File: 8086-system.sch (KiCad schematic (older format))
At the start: 2 parts

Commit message: created 8284A clock generator block
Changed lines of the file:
@@
 $Descr A4 11693 8268
 encoding utf-8
-Sheet 1 3
+Sheet 1 4
 Title "8086-system"
 Date ""
@@
 F0 "external-connectors" 50
 F1 "external-connectors.sch" 50
-F2 "ADDRESS_BUS" O L 8950 3100 50
-F3 "CLK" I L 8950 3450 50
-F4 "~BHE" I L 8950 3600 50
-F5 "~MRDC" I R 9900 3250 50
-F6 "~MWTC" I R 9900 3350 50
-F7 "~IORC" I R 9900 3450 50
-F8 "~IOWC" I R 9900 3550 50
-F9 "DATA_BUS" B L 8950 3200 50
+F2 "CLK" I L 8950 3500 50
+F3 "~BHE" I L 8950 3300 50
+F4 "~MRDC" I R 9900 3250 50
+F5 "~MWTC" I R 9900 3350 50
+F6 "~IORC" I R 9900 3450 50
+F7 "~IOWC" I R 9900 3550 50
+F8 "DATA_BUS" B L 8950 3200 50
+F9 "RESET" I L 8950 3600 50
+F10 "ADDRESS_BUS" I L 8950 3100 50
 $EndSheet
 Text Label 2000 3350 0    50   ~ 0
@@
 Text Label 1150 3400 2    50   ~ 0
 RESET
-Text Label 1150 3600 2    50   ~ 0
-~TEST
 Text Label 1150 3700 2    50   ~ 0
 HOLD
@@
 Text Label 1150 4200 2    50   ~ 0
 ~INTA
-Text Label 8950 3450 2    50   ~ 0
+Text Label 8950 3500 2    50   ~ 0
 CLK
-Text Label 8950 3600 2    50   ~ 0
+Text Label 8950 3300 2    50   ~ 0
 ~BHE
 Text Label 9900 3250 0    50   ~ 0
@@
 $EndComp
 $Comp
-L power:GND #PWR?
+L power:GND #PWR0101
 U 1 1 62850EC1
 P 1500 7450
-F 0 "#PWR?" H 1500 7200 50  0001 C CNN
+F 0 "#PWR0101" H 1500 7200 50  0001 C CNN
 F 1 "GND" H 1505 7277 50  0000 C CNN
 F 2 "" H 1500 7450 50  0001 C CNN
@@
 $EndComp
 $Comp
-L power:VCC #PWR?
+L power:VCC #PWR0102
 U 1 1 62851416
 P 1900 7150
-F 0 "#PWR?" H 1900 7000 50  0001 C CNN
+F 0 "#PWR0102" H 1900 7000 50  0001 C CNN
 F 1 "VCC" H 1915 7323 50  0000 C CNN
 F 2 "" H 1900 7150 50  0001 C CNN
@@
 	1350 7450 1500 7450
 Connection ~ 1500 7450
+$Sheet
+S 1700 1050 750  550
+U 6193175A
+F0 "clock-generator" 50
+F1 "clock-generator.sch" 50
+F2 "PCLK" O R 2450 1250 50
+F3 "CLK" O R 2450 1150 50
+F4 "RESET" O R 2450 1400 50
+F5 "READY" O R 2450 1500 50
+F6 "RDY1" I L 1700 1150 50
+F7 "RDY2" I L 1700 1400 50
+$EndSheet
+Text Label 2450 1150 0    50   ~ 0
+CLK
+Text Label 2450 1250 0    50   ~ 0
+PCLK
+Text Label 2450 1500 0    50   ~ 0
+READY
+Text Label 2450 1400 0    50   ~ 0
+RESET
+Wire Wire Line
+	1150 3600 800  3600
+$Comp
+L power:GND #PWR0103
+U 1 1 61966AE7
+P 800 3600
+F 0 "#PWR0103" H 800 3350 50  0001 C CNN
+F 1 "GND" H 805 3427 50  0000 C CNN
+F 2 "" H 800 3600 50  0001 C CNN
+F 3 "" H 800 3600 50  0001 C CNN
+	1    800  3600
+	1    0    0    -1
+$EndComp
+Wire Wire Line
+	1400 1150 1400 1400
+$Comp
+L power:VCC #PWR0104
+U 1 1 61967609
+P 1400 1150
+F 0 "#PWR0104" H 1400 1000 50  0001 C CNN
+F 1 "VCC" H 1415 1323 50  0000 C CNN
+F 2 "" H 1400 1150 50  0001 C CNN
+F 3 "" H 1400 1150 50  0001 C CNN
+	1    1400 1150
+	1    0    0    -1
+$EndComp
+Wire Wire Line
+	1700 1400 1400 1400
+Wire Wire Line
+	1700 1150 1400 1150
+Connection ~ 1400 1150
+Text Label 8950 3600 2    50   ~ 0
+RESET
 $EndSCHEMATC

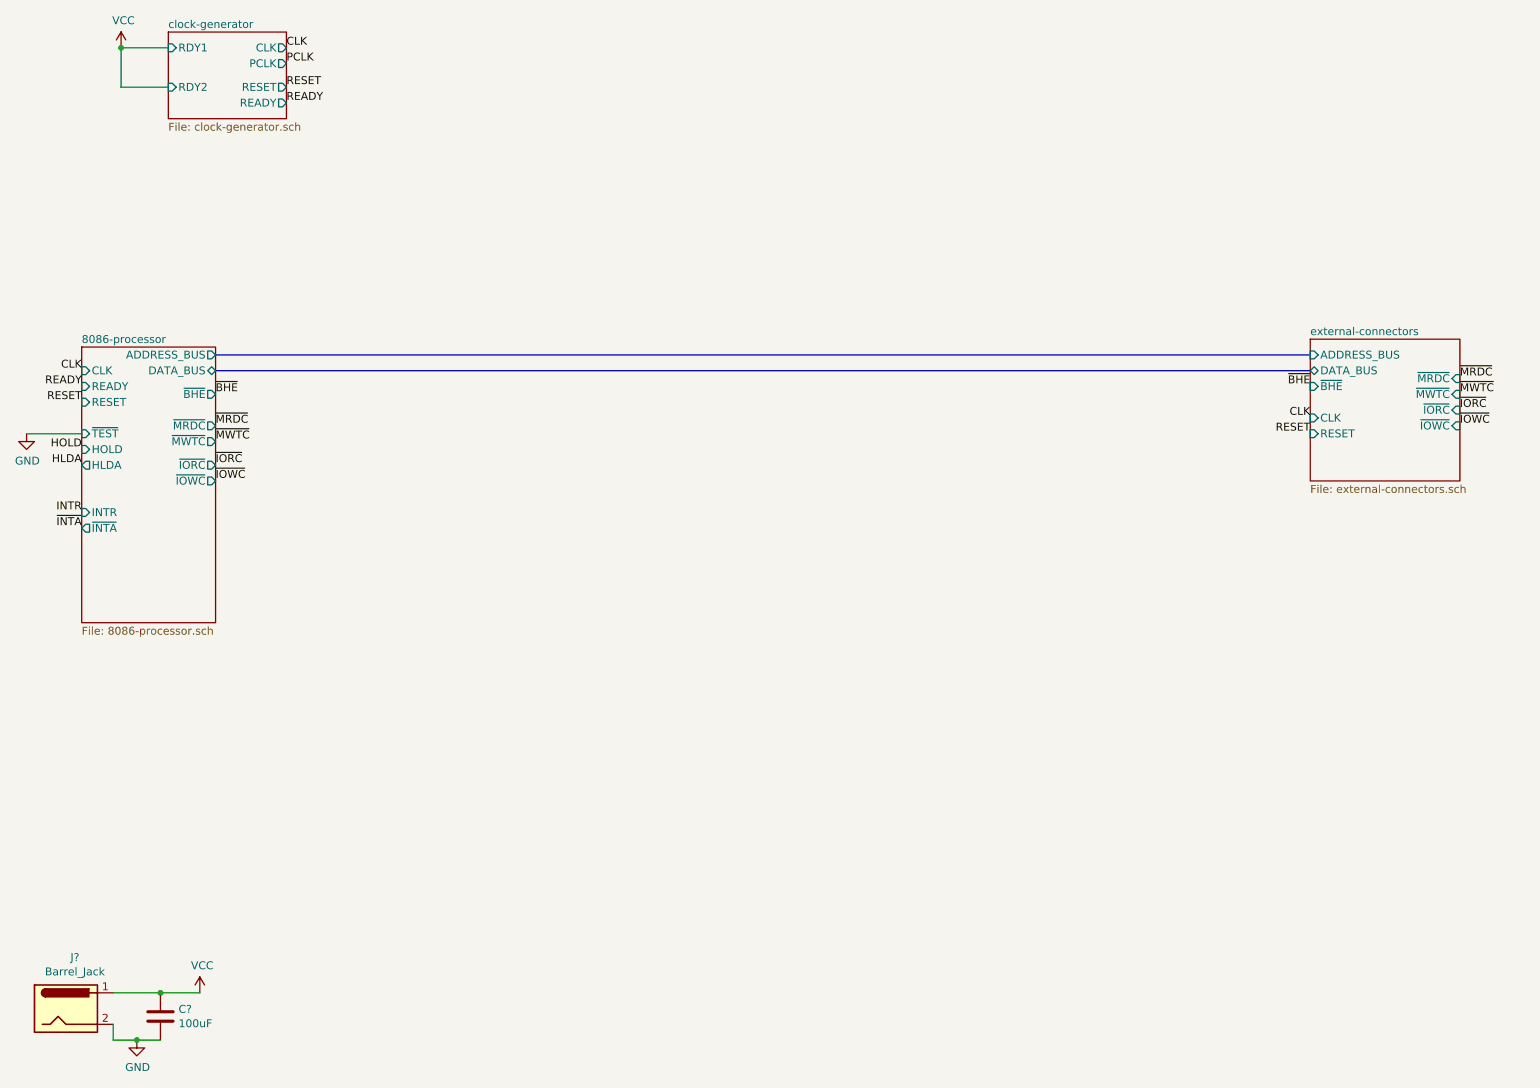
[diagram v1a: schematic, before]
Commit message: created 28F010 CMOS flash block; improved power decoupling; added M/~IO pin from 8086 sheet; reduced no. of logic gates in 8086 processor block; added +12V; moved input power to external-connectors sheet; annotated schematics
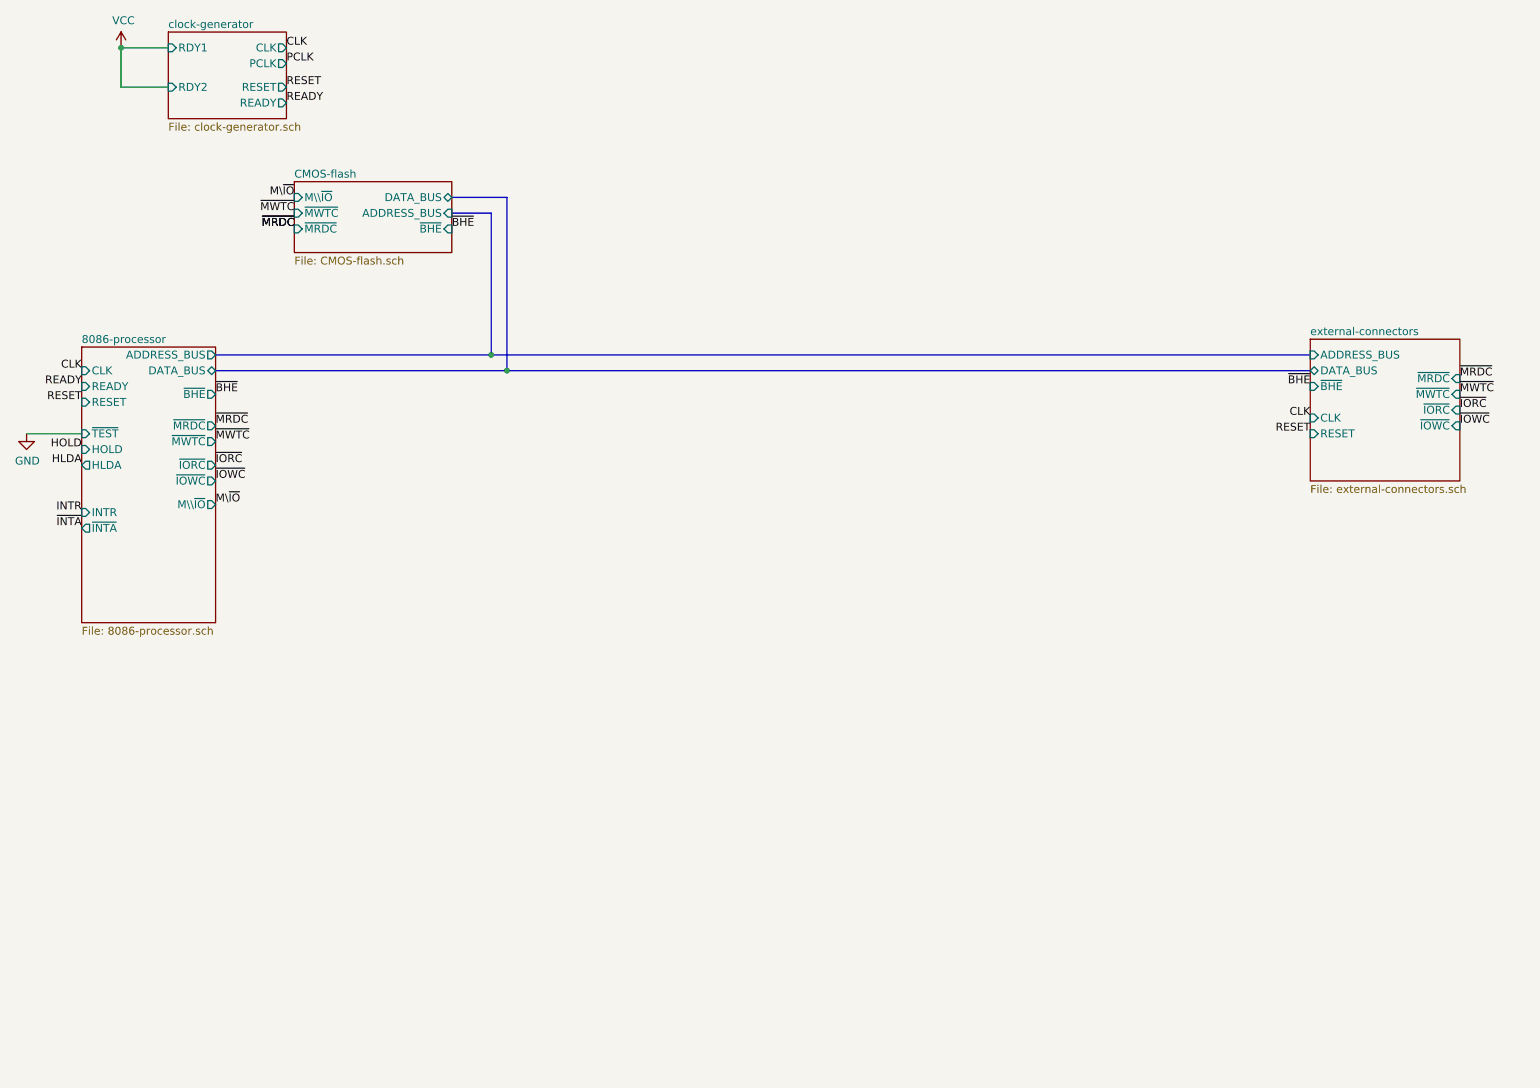
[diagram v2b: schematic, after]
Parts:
- removed C?: 100uF, symbol Device:C
- removed J?: Barrel_Jack, symbol Connector:Barrel_Jack
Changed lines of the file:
@@
 $Descr A4 11693 8268
 encoding utf-8
-Sheet 1 4
+Sheet 1 5
 Title "8086-system"
 Date ""
@@
 F15 "~IOWC" O R 2000 3900 50
 F16 "DATA_BUS" B R 2000 3200 50
+F17 "M\\~IO" O R 2000 4050 50
 $EndSheet
 $Sheet
@@
 ~IOWC
 Wire Bus Line
-	2000 3100 8950 3100
+	2000 3100 3750 3100
 Wire Bus Line
-	2000 3200 8950 3200
-$Comp
-L Connector:Barrel_Jack J?
-U 1 1 6284FC4C
-P 1050 7250
-F 0 "J?" H 1107 7575 50  0000 C CNN
-F 1 "Barrel_Jack" H 1107 7484 50  0000 C CNN
-F 2 "" H 1100 7210 50  0001 C CNN
-F 3 "~" H 1100 7210 50  0001 C CNN
-	1    1050 7250
-	1    0    0    -1
-$EndComp
-$Comp
-L power:GND #PWR0101
-U 1 1 62850EC1
-P 1500 7450
-F 0 "#PWR0101" H 1500 7200 50  0001 C CNN
-F 1 "GND" H 1505 7277 50  0000 C CNN
-F 2 "" H 1500 7450 50  0001 C CNN
-F 3 "" H 1500 7450 50  0001 C CNN
-	1    1500 7450
-	1    0    0    -1
-$EndComp
-$Comp
-L power:VCC #PWR0102
-U 1 1 62851416
-P 1900 7150
-F 0 "#PWR0102" H 1900 7000 50  0001 C CNN
-F 1 "VCC" H 1915 7323 50  0000 C CNN
-F 2 "" H 1900 7150 50  0001 C CNN
-F 3 "" H 1900 7150 50  0001 C CNN
-	1    1900 7150
-	1    0    0    -1
-$EndComp
-$Comp
-L Device:C C?
-U 1 1 62851EC8
-P 1650 7300
-F 0 "C?" H 1765 7346 50  0000 L CNN
-F 1 "100uF" H 1765 7255 50  0000 L CNN
-F 2 "" H 1688 7150 50  0001 C CNN
-F 3 "~" H 1650 7300 50  0001 C CNN
-	1    1650 7300
-	1    0    0    -1
-$EndComp
-Wire Wire Line
-	1350 7150 1650 7150
-Wire Wire Line
-	1900 7150 1650 7150
-Connection ~ 1650 7150
-Wire Wire Line
-	1650 7450 1500 7450
-Wire Wire Line
-	1350 7350 1350 7450
-Wire Wire Line
-	1350 7450 1500 7450
-Connection ~ 1500 7450
+	2000 3200 3850 3200
 $Sheet
 S 1700 1050 750  550
@@
 Text Label 8950 3600 2    50   ~ 0
 RESET
+$Sheet
+S 2500 2000 1000 450
+U 61A2E343
+F0 "CMOS-flash" 50
+F1 "CMOS-flash.sch" 50
+F2 "~MRDC" I L 2500 2300 50
+F3 "DATA_BUS" B R 3500 2100 50
+F4 "ADDRESS_BUS" I R 3500 2200 50
+F5 "M\\~IO" I L 2500 2100 50
+F6 "~BHE" I R 3500 2300 50
+F7 "~MWTC" I L 2500 2200 50
+$EndSheet
+Text Label 3500 2300 0    50   ~ 0
+~BHE
+Wire Bus Line
+	3500 2200 3750 2200
+Wire Bus Line
+	3750 2200 3750 3100
+Connection ~ 3750 3100
+Wire Bus Line
+	3750 3100 8950 3100
+Wire Bus Line
+	3500 2100 3850 2100
+Wire Bus Line
+	3850 2100 3850 3200
+Connection ~ 3850 3200
+Wire Bus Line
+	3850 3200 8950 3200
+Text Label 2500 2300 2    50   ~ 0
+~MRDC
+Text Label 2500 2300 2    50   ~ 0
+~MRDC
+Text Label 2500 2200 2    50   ~ 0
+~MWTC
+Text Label 2500 2100 2    50   ~ 0
+M\~IO
+Text Label 2000 4050 0    50   ~ 0
+M\~IO
 $EndSCHEMATC

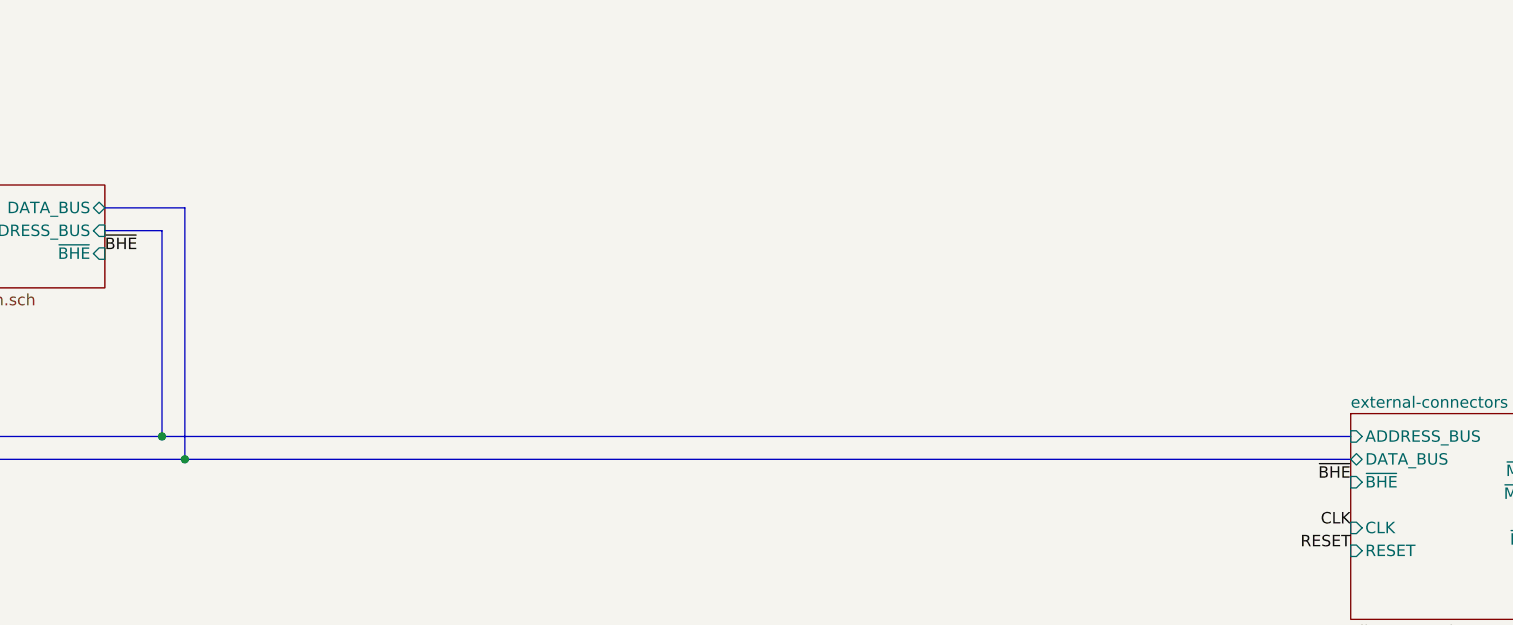
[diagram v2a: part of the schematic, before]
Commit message: created 16550 UART interface block
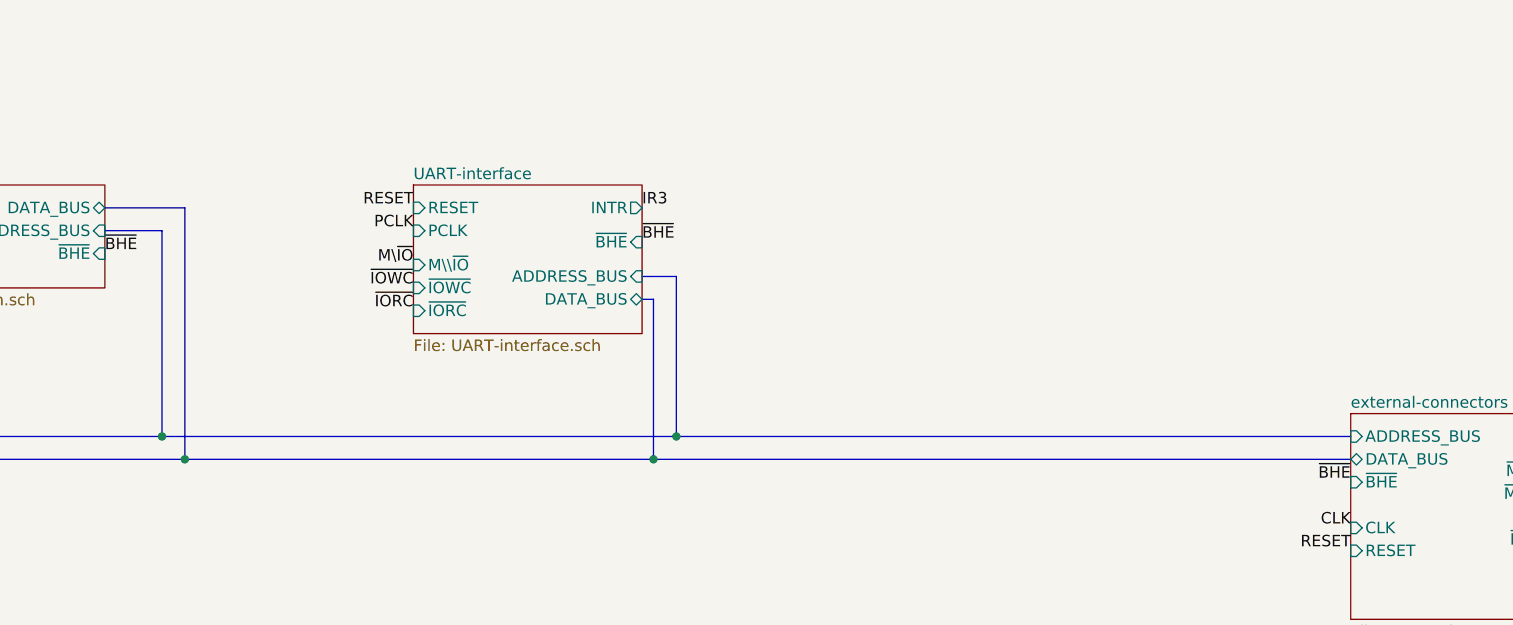
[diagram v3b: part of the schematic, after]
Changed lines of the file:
@@
 $Descr A4 11693 8268
 encoding utf-8
-Sheet 1 5
+Sheet 1 6
 Title "8086-system"
 Date ""
@@
 Connection ~ 3750 3100
 Wire Bus Line
-	3750 3100 8950 3100
+	3750 3100 6000 3100
 Wire Bus Line
 	3500 2100 3850 2100
@@
 Connection ~ 3850 3200
 Wire Bus Line
-	3850 3200 8950 3200
+	3850 3200 5900 3200
 Text Label 2500 2300 2    50   ~ 0
 ~MRDC
@@
 Text Label 2000 4050 0    50   ~ 0
 M\~IO
+$Sheet
+S 4850 2000 1000 650
+U 61A42887
+F0 "UART-interface" 50
+F1 "UART-interface.sch" 50
+F2 "INTR" O R 5850 2100 50
+F3 "~IORC" I L 4850 2550 50
+F4 "~IOWC" I L 4850 2450 50
+F5 "PCLK" I L 4850 2200 50
+F6 "DATA_BUS" B R 5850 2500 50
+F7 "RESET" I L 4850 2100 50
+F8 "ADDRESS_BUS" I R 5850 2400 50
+F9 "M\\~IO" I L 4850 2350 50
+F10 "~BHE" I R 5850 2250 50
+$EndSheet
+Text Label 5850 2250 0    50   ~ 0
+~BHE
+Text Label 5850 2100 0    50   ~ 0
+IR3
+Wire Bus Line
+	5850 2500 5900 2500
+Wire Bus Line
+	5900 2500 5900 3200
+Connection ~ 5900 3200
+Wire Bus Line
+	5900 3200 8950 3200
+Wire Bus Line
+	5850 2400 6000 2400
+Wire Bus Line
+	6000 2400 6000 3100
+Connection ~ 6000 3100
+Wire Bus Line
+	6000 3100 8950 3100
+Text Label 4850 2350 2    50   ~ 0
+M\~IO
+Text Label 4850 2450 2    50   ~ 0
+~IOWC
+Text Label 4850 2550 2    50   ~ 0
+~IORC
+Text Label 4850 2200 2    50   ~ 0
+PCLK
+Text Label 4850 2100 2    50   ~ 0
+RESET
 $EndSCHEMATC
